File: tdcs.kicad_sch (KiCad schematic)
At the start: 18 parts, among them J1 Electrodes, M1 0-2.0mA, Q1 MMBFJ111, U1 LM334Z, U2 LT1026

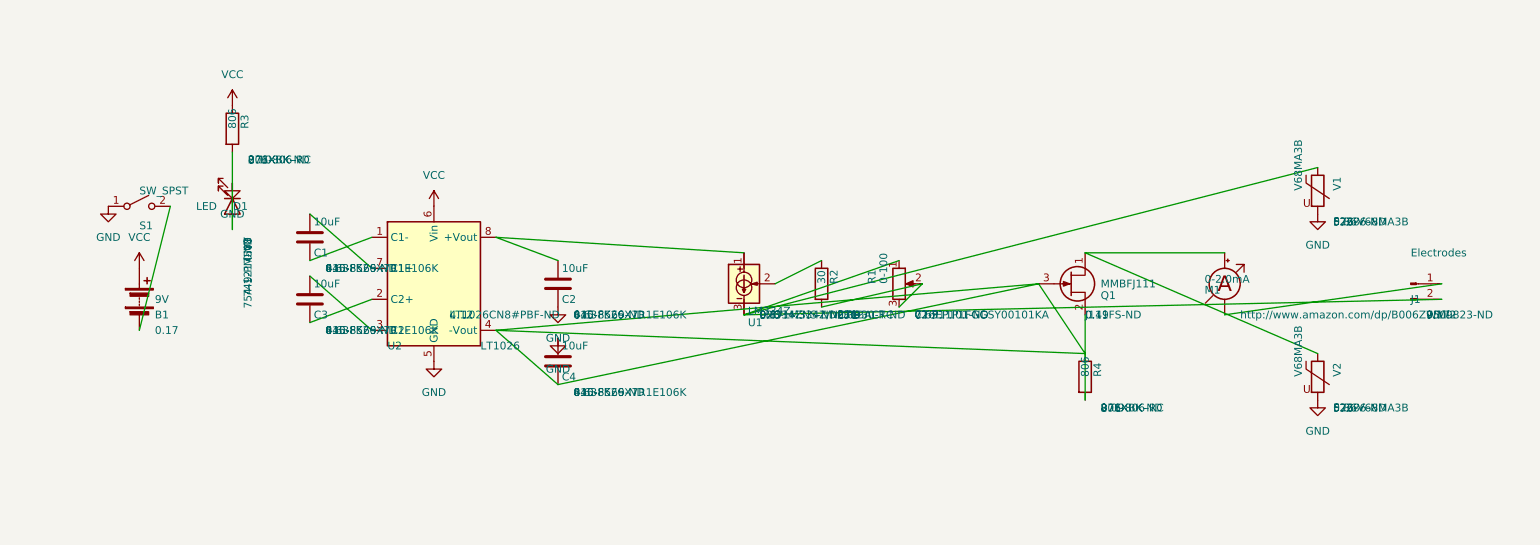
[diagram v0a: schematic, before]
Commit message: Add PWR_FLAG symbols to silence ERC power-not-driven errors
KiCad ERC requires explicit PWR_FLAG markers on power nets to
confirm they are intentionally driven. Added one on GND and one
on VCC.
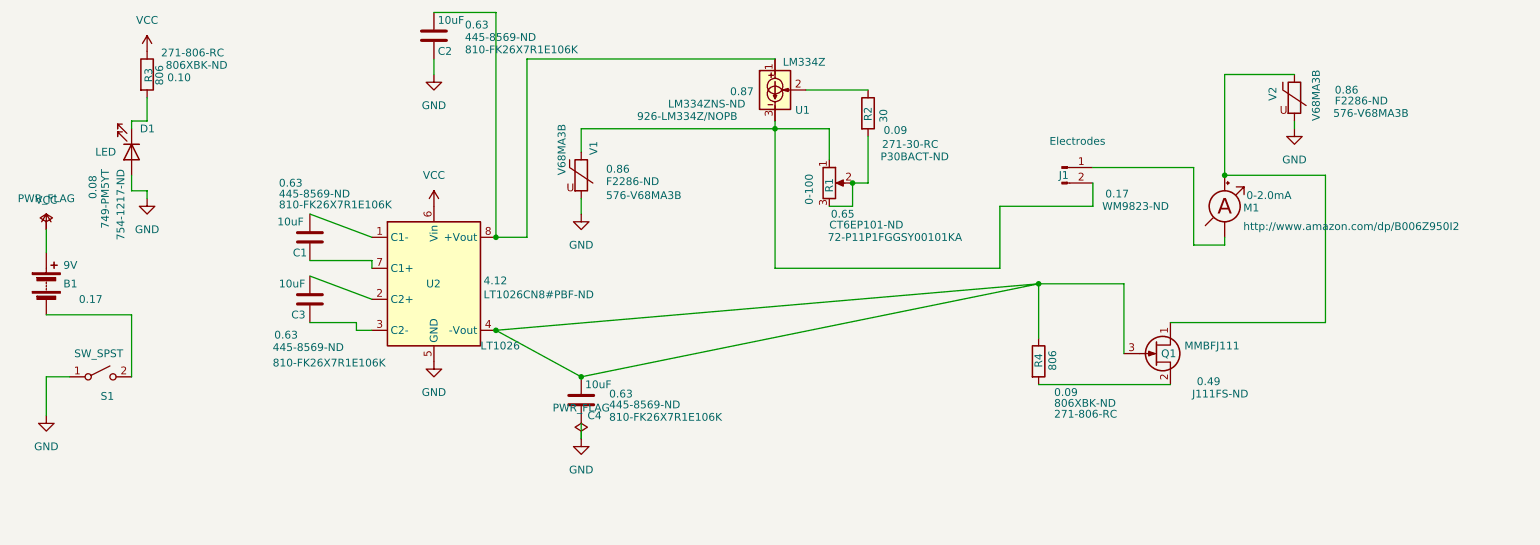
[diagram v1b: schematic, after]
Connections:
- net GND: now also C4.2, D1.2 (A); no longer C4.1, D1.1 (K)
- net at R3.2: now also D1.1 (K); no longer D1.2 (A)
- net at U2.1 (C1-): now also C1.1; no longer C1.2
- net at U2.2 (C2+): now also C3.1; no longer C3.2
- net at U2.3 (C2-): now also C3.2; no longer C3.1
- net at Q1.3 (G), R4.1, U2.4 (-Vout): now also C4.1; no longer C4.2
- net at U2.7 (C1+): now also C1.2; no longer C1.1
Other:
- moved on the sheet: B1, C2, C4, D1, J1, M1, Q1, R1, R2, R3, R4, S1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

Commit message: Rearrange schematic layout for readability, fix LED orientation
Components repositioned in KiCad GUI for clearer signal flow.
Fixed D1 (LED) orientation — was reverse-biased after move.
KiCad project file updated with DRC/ERC settings from GUI.
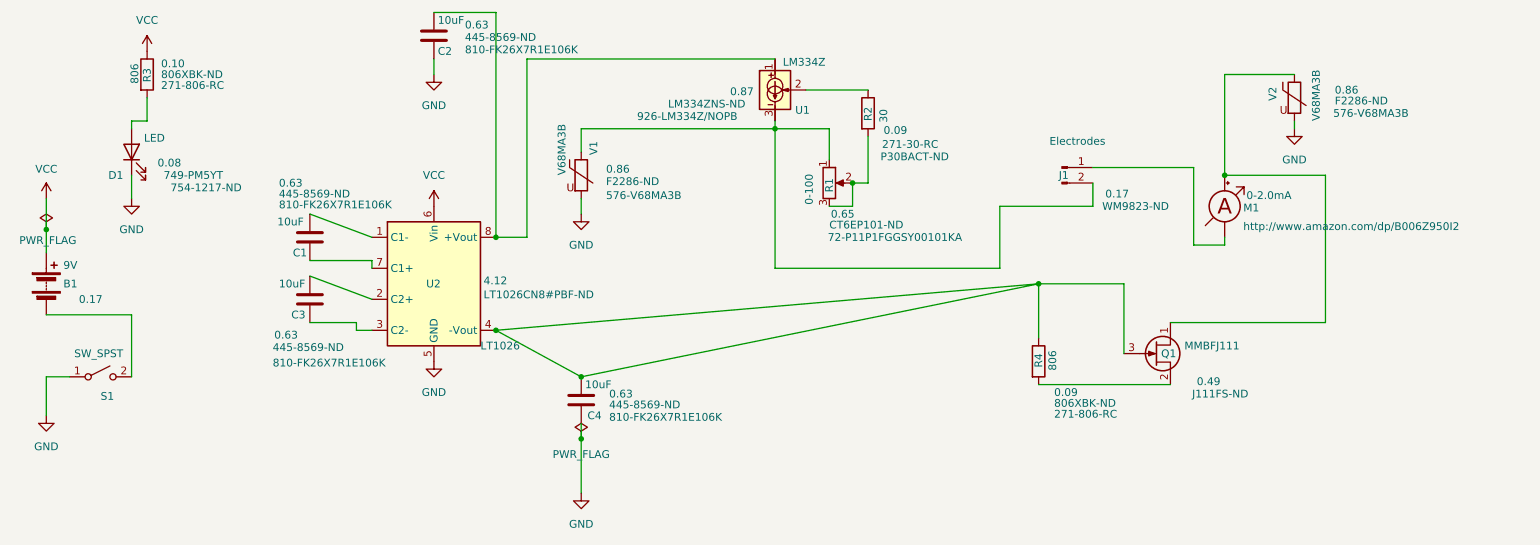
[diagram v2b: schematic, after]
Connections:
- net GND: now also D1.1 (K); no longer D1.2 (A)
- net at R3.2: now also D1.2 (A); no longer D1.1 (K)
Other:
- moved on the sheet: D1

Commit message: Update supplier part numbers and pricing to current (March 2026)
- R2: DigiKey P30BACT-ND (obsolete) → 30QBK-ND (YAGEO CFR-25JB-52-30R)
- R2: Mouser 271-30-RC (discontinued) → 603-CFR-25JB-52-30R
- D1: Mouser 749-PM5YT (wrong part) → 604-WP3A8GD (correct green 3mm LED)
- U2: added Mouser 584-LT1026CN8#PBF
- Q1: added Mouser 512-J111
- R3/R4: Mouser updated to 603-MFR-25FBF52-806R
- M1: Amazon link updated (old listing dead) → B086Q1HT28
- All prices updated to current single-quantity pricing
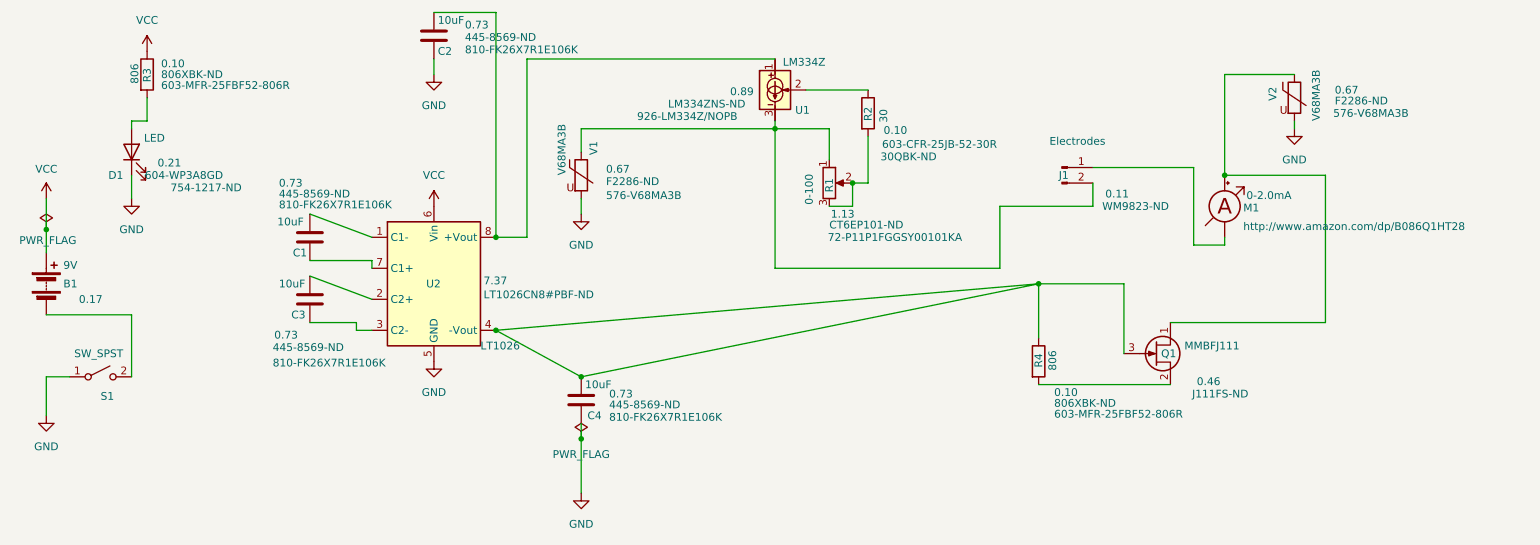
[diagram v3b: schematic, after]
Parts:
- C1, C2, C3, C4: Price 0.63 -> 0.73
- D1: Mouser 749-PM5YT -> 604-WP3A8GD; Price 0.08 -> 0.21
- J1: Price 0.17 -> 0.11
- M1: Amazon_Link http://www.amazon.com/dp/B006Z950I2 -> http://www.amazon.com/dp/B086Q1HT28
- Q1: Mouser (none) -> 512-J111; Price 0.49 -> 0.46
- R1: Price 0.65 -> 1.13
- R2: DigiKey P30BACT-ND -> 30QBK-ND; Mouser 271-30-RC -> 603-CFR-25JB-52-30R; Price 0.09 -> 0.10
- R3: Mouser 271-806-RC -> 603-MFR-25FBF52-806R
- R4: Mouser 271-806-RC -> 603-MFR-25FBF52-806R; Price 0.09 -> 0.10
- U1: Price 0.87 -> 0.89
- U2: Mouser (none) -> 584-LT1026CN8#PBF; Price 4.12 -> 7.37
- V1, V2: Price 0.86 -> 0.67
